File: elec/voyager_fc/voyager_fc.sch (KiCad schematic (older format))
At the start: 173 parts, among them J1 Raspberry Pi 5 Connector, J10 PWM Signal Rail 1, J11 BM03B-GHS-TBT_LF__SN__N_, J12 BM03B-GHS-TBT_LF__SN__N_, J13 BM03B-GHS-TBT_LF__SN__N_, J14 BM03B-GHS-TBT_LF__SN__N_, J15 Pi Power Connect, J16 AUX Power Connect, J17 BM04B-GHS-TBT_LF__SN__N_, J18 BM04B-GHS-TBT_LF__SN__N_, J19 BM04B-GHS-TBT_LF__SN__N_, J2 BM06B-GHS-TBT_LF__SN__N_, J20 BM04B-GHS-TBT_LF__SN__N_, J21 AUX Leak, J22 BM02B-GHS-TBT_LF__SN__N_, J23 BM02B-GHS-TBT_LF__SN__N_, J24 BM02B-GHS-TBT_LF__SN__N_, J3 BM06B-GHS-TBT_LF__SN__N_, J4 BM06B-GHS-TBT_LF__SN__N_, J5 PWM Power Rail 2, J6 PWM GND Rail 2, J7 PWM Signal Rail 2, J8 PWM Power Rail 1, J9 PWM GND Rail 1, Q1 BSS138, Q2 BSS138, Q3 MMBT3906, U1 BME680, U10 LTC4311CDC_TRMPBF, U11 AMS1117-3.3, U12 TCA9548APWR, U13 TXS0102YZP, U14 TXS0102YZP, U15 TXS0102YZP, U16 TXS0102YZP, U17 ICM-20948, U2 PCA9685PW, U3 PCA9685PW, U4 ADS1015IDGS, U5 TPS2121RUXR, U6 AMS1117-1.8, U7 LTC4311CDC_TRMPBF, U8 LTC4311CDC_TRMPBF, U9 LTC4311CDC_TRMPBF, X1 SG-8002CE

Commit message: Start schematic makeover with proper hierarchy
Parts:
- removed C1, C10, C11, C12, C13, C14, C15, C16, C17, C18, C19, C2, C20, C21, C25, C26, C27, C28, C30, C31, C32, C5, C8, C9: 10uF, Capacitor_SMD:C_0805_2012Metric, symbol Device:C_Small
- removed C22: 1nF, Capacitor_SMD:C_0603_1608Metric, symbol Device:C_Small
- removed C23, C29: 1uF, Capacitor_SMD:C_0603_1608Metric, symbol Device:C_Small
- removed C24, C33: 10uF, Capacitor_SMD:C_0603_1608Metric, symbol Device:C_Small
- removed C3, C6: 0.1uF, Capacitor_SMD:C_0603_1608Metric, symbol Device:C_Small
- removed C34, C35, C36, C37, C46, C47, C48, C49: 10uF, Capacitor_SMD:C_0504_1310Metric, symbol Device:C_Small
- removed C38, C39, C40, C41: 0.1uF, Capacitor_SMD:C_0504_1310Metric, symbol Device:C_Small
- removed C4, C7: 4700uF, Capacitor_THT:CP_Radial_D10.0mm_P5.00mm, symbol Device:C
- removed C54: 0.1uf, Capacitor_SMD:C_0603_1608Metric, symbol Device:C_Small
- removed D4: WHITE, LED_SMD:LED_0603_1608Metric, symbol Device:LED
- removed J10: PWM Signal Rail 1, Connector_PinHeader_2.54mm:PinHeader_1x16_P2.54mm_Vertical, symbol Connector_Generic:Conn_01x16
- removed J5: PWM Power Rail 2, Connector_PinHeader_2.54mm:PinHeader_1x16_P2.54mm_Vertical, symbol Connector_Generic:Conn_01x16
- removed J6: PWM GND Rail 2, Connector_PinHeader_2.54mm:PinHeader_1x16_P2.54mm_Vertical, symbol Connector_Generic:Conn_01x16
- removed J7: PWM Signal Rail 2, Connector_PinHeader_2.54mm:PinHeader_1x16_P2.54mm_Vertical, symbol Connector_Generic:Conn_01x16
- removed J8: PWM Power Rail 1, Connector_PinHeader_2.54mm:PinHeader_1x16_P2.54mm_Vertical, symbol Connector_Generic:Conn_01x16
- removed J9: PWM GND Rail 1, Connector_PinHeader_2.54mm:PinHeader_1x16_P2.54mm_Vertical, symbol Connector_Generic:Conn_01x16
- removed Q1, Q2: BSS138, Package_TO_SOT_SMD:SOT-23, symbol Transistor_FET:BSS138
- removed Q3: MMBT3906, Package_TO_SOT_SMD:SOT-23, symbol Transistor_BJT:MMBT3906
- removed R10, R11, R12, R13, R14, R15, R16, R17, R18, R19, R20, R23, R24, R25, R26, R27, R28, R29, R30, R31, R32, R33, R34, R35, R36, R37, R38, R5, R6, R7, R70, R8, R9: 220, Resistor_SMD:R_0603_1608Metric, symbol Device:R_Small
- removed R21: 200, Resistor_SMD:R_0603_1608Metric, symbol Device:R_Small
- removed R22, R4, R64, R65, R66, R67: 10k, Resistor_SMD:R_0603_1608Metric, symbol Device:R_Small
- removed R39: 19.6k, Resistor_SMD:R_0603_1608Metric, symbol Device:R_Small
- removed R40, R41, R42, R43, R46, R52, R53, R54, R55, R56, R57, R58, R59, R60, R61, R62, R63: 10k, Resistor_SMD:R_0402_1005Metric, symbol Device:R_Small
- removed R44: 4.99k, Resistor_SMD:R_0603_1608Metric, symbol Device:R_Small
- removed R45, R48: 1.15k, Resistor_SMD:R_0603_1608Metric, symbol Device:R_Small
- removed R47: 4.99K, Resistor_SMD:R_0603_1608Metric, symbol Device:R_Small
- removed R49: 4.32k, Resistor_SMD:R_0603_1608Metric, symbol Device:R_Small
- removed R50: 10.2k, Resistor_SMD:R_0603_1608Metric, symbol Device:R_Small
- removed R51: 36.5k, Resistor_SMD:R_0603_1608Metric, symbol Device:R_Small
- removed R68: 20K, Resistor_SMD:R_0603_1608Metric, symbol Device:R_Small
- removed R69: 1K, Resistor_SMD:R_0603_1608Metric, symbol Device:R_Small
- removed U1: BME680, Package_LGA:Bosch_LGA-8_3x3mm_P0.8mm_ClockwisePinNumbering, symbol Sensor:BME680
- removed U10, U7, U8, U9: LTC4311CDC_TRMPBF, DFN-6_DC, symbol LTC4311CDC_TRMPBF:LTC4311CDC_TRMPBF
- removed U11: AMS1117-3.3, Package_TO_SOT_SMD:SOT-223-3_TabPin2, symbol Regulator_Linear:AMS1117-3.3
- removed U12: TCA9548APWR, Package_SO:TSSOP-24_4.4x7.8mm_P0.65mm, symbol Interface_Expansion:TCA9548APWR
- removed U13, U14, U15, U16: TXS0102YZP, Package_BGA:Texas_DSBGA-8_0.9x1.9mm_Layout2x4_P0.5mm, symbol Logic_LevelTranslator:TXS0102YZP
- removed U17: ICM-20948, Sensor_Motion:InvenSense_QFN-24_3x3mm_P0.4mm, symbol Sensor_Motion:ICM-20948
- removed U2, U3: PCA9685PW, Package_SO:TSSOP-28_4.4x9.7mm_P0.65mm, symbol Driver_LED:PCA9685PW
- removed U4: ADS1015IDGS, Package_SO:TSSOP-10_3x3mm_P0.5mm, symbol Analog_ADC:ADS1015IDGS
- removed U5: TPS2121RUXR, IC_TPS2121RUXR, symbol TPS2121RUXR:TPS2121RUXR
- removed U6: AMS1117-1.8, Package_TO_SOT_SMD:SOT-223-3_TabPin2, symbol Regulator_Linear:AMS1117-1.8
- removed X1: SG-8002CE, Oscillator:Oscillator_SMD_SeikoEpson_SG8002CE-4Pin_3.2x2.5mm, symbol Oscillator:SG-8002CE
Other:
- moved on the sheet: C42, C43, C44, C45, C50, C51, C52, C53, J11, J12, J13, J14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

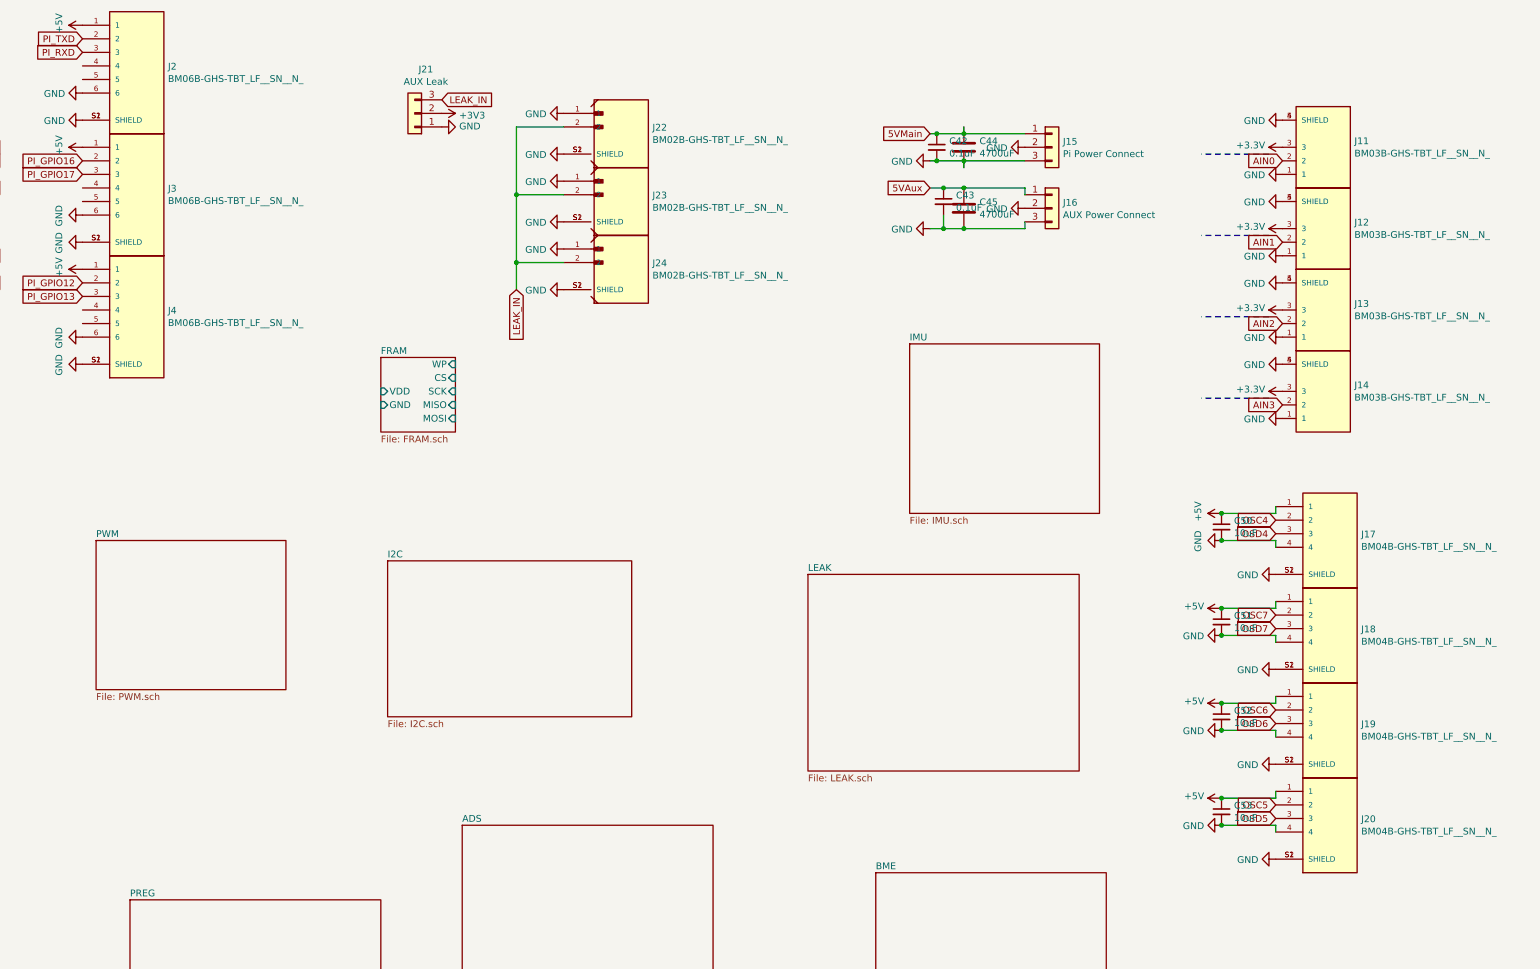
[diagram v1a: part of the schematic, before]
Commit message: Move connectors inside schematics
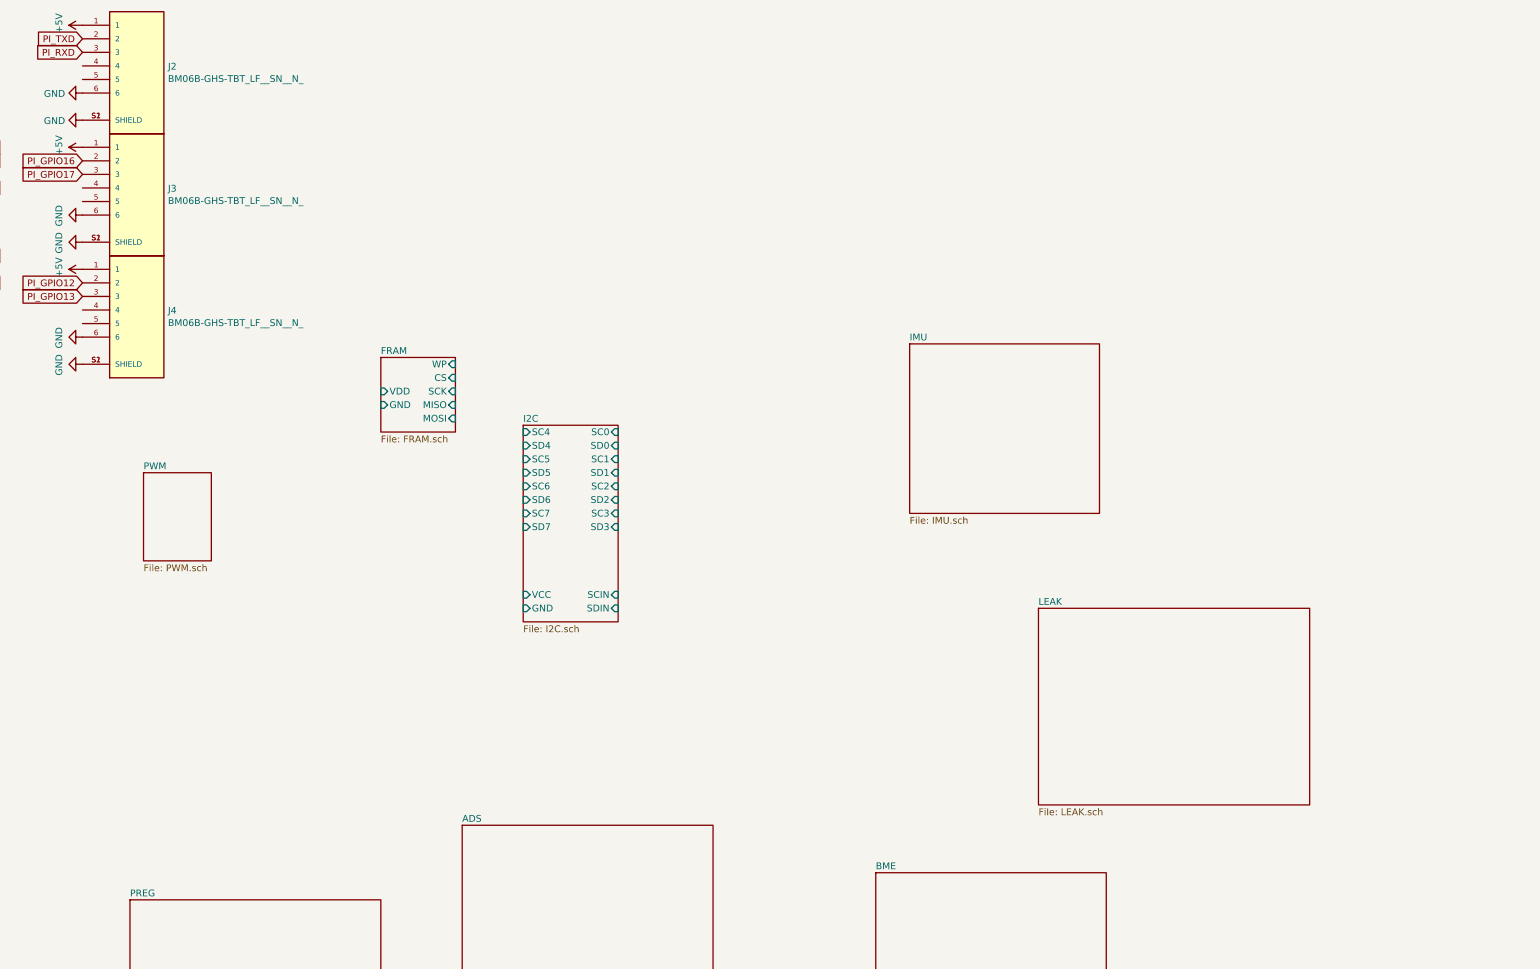
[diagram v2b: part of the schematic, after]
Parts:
- removed C42, C43: 0.1uF, Capacitor_SMD:C_0603_1608Metric, symbol Device:C_Small
- removed C44, C45: 4700uF, Capacitor_THT:CP_Radial_D10.0mm_P5.00mm, symbol Device:C
- removed C50, C51, C52, C53: 10uF, Capacitor_SMD:C_0504_1310Metric, symbol Device:C_Small
- removed J11, J12, J13, J14: BM03B-GHS-TBT_LF__SN__N_, CONN_BM03B-GHS-TBT_LF__SN__N_, symbol BM03B-GHS-TBT_LF__SN__N_:BM03B-GHS-TBT_LF__SN__N_
- removed J15: Pi Power Connect, Connector_PinHeader_2.54mm:PinHeader_1x03_P2.54mm_Vertical, symbol Connector_Generic:Conn_01x03
- removed J16: AUX Power Connect, Connector_PinHeader_2.54mm:PinHeader_1x03_P2.54mm_Vertical, symbol Connector_Generic:Conn_01x03
- removed J17, J18, J19, J20: BM04B-GHS-TBT_LF__SN__N_, JST_BM04B-GHS-TBT_LF__SN__N_, symbol BM04B-GHS-TBT_LF__SN__N_:BM04B-GHS-TBT_LF__SN__N_
- removed J21: AUX Leak, Connector_PinHeader_2.54mm:PinHeader_1x03_P2.54mm_Vertical, symbol Connector_Generic:Conn_01x03
- removed J22, J23, J24: BM02B-GHS-TBT_LF__SN__N_, JST_BM02B-GHS-TBT_LF__SN__N_, symbol BM02B-GHS-TBT_LF__SN__N_:BM02B-GHS-TBT_LF__SN__N_

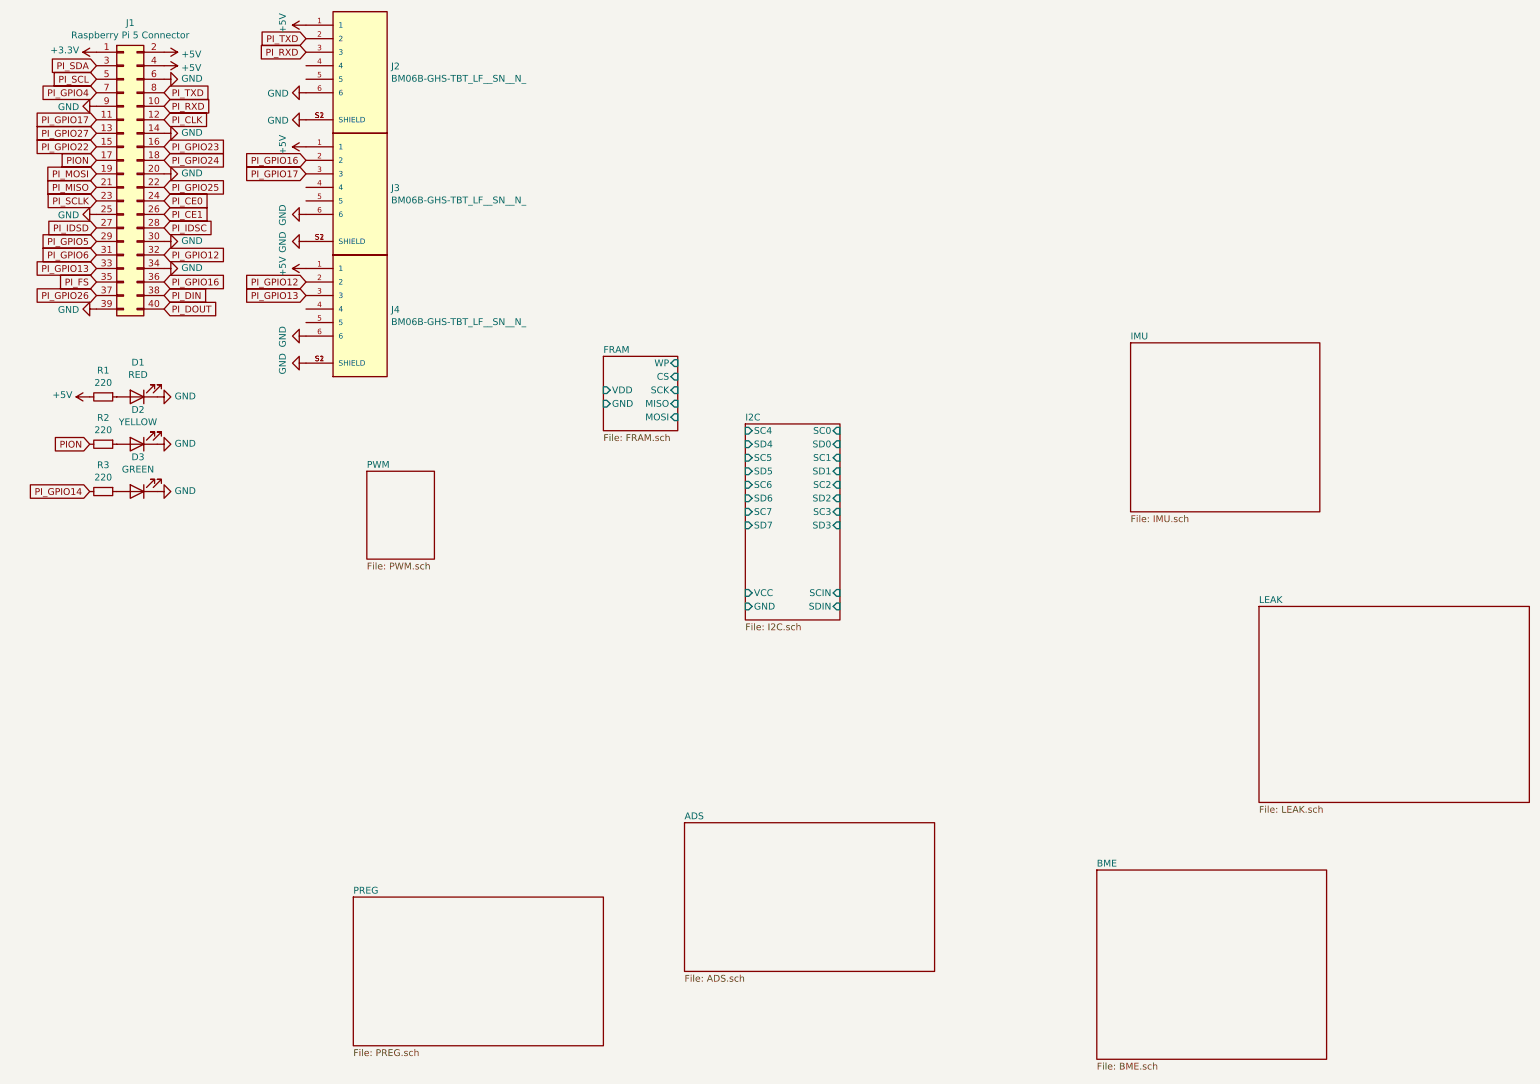
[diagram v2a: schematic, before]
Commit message: Place all components and start route
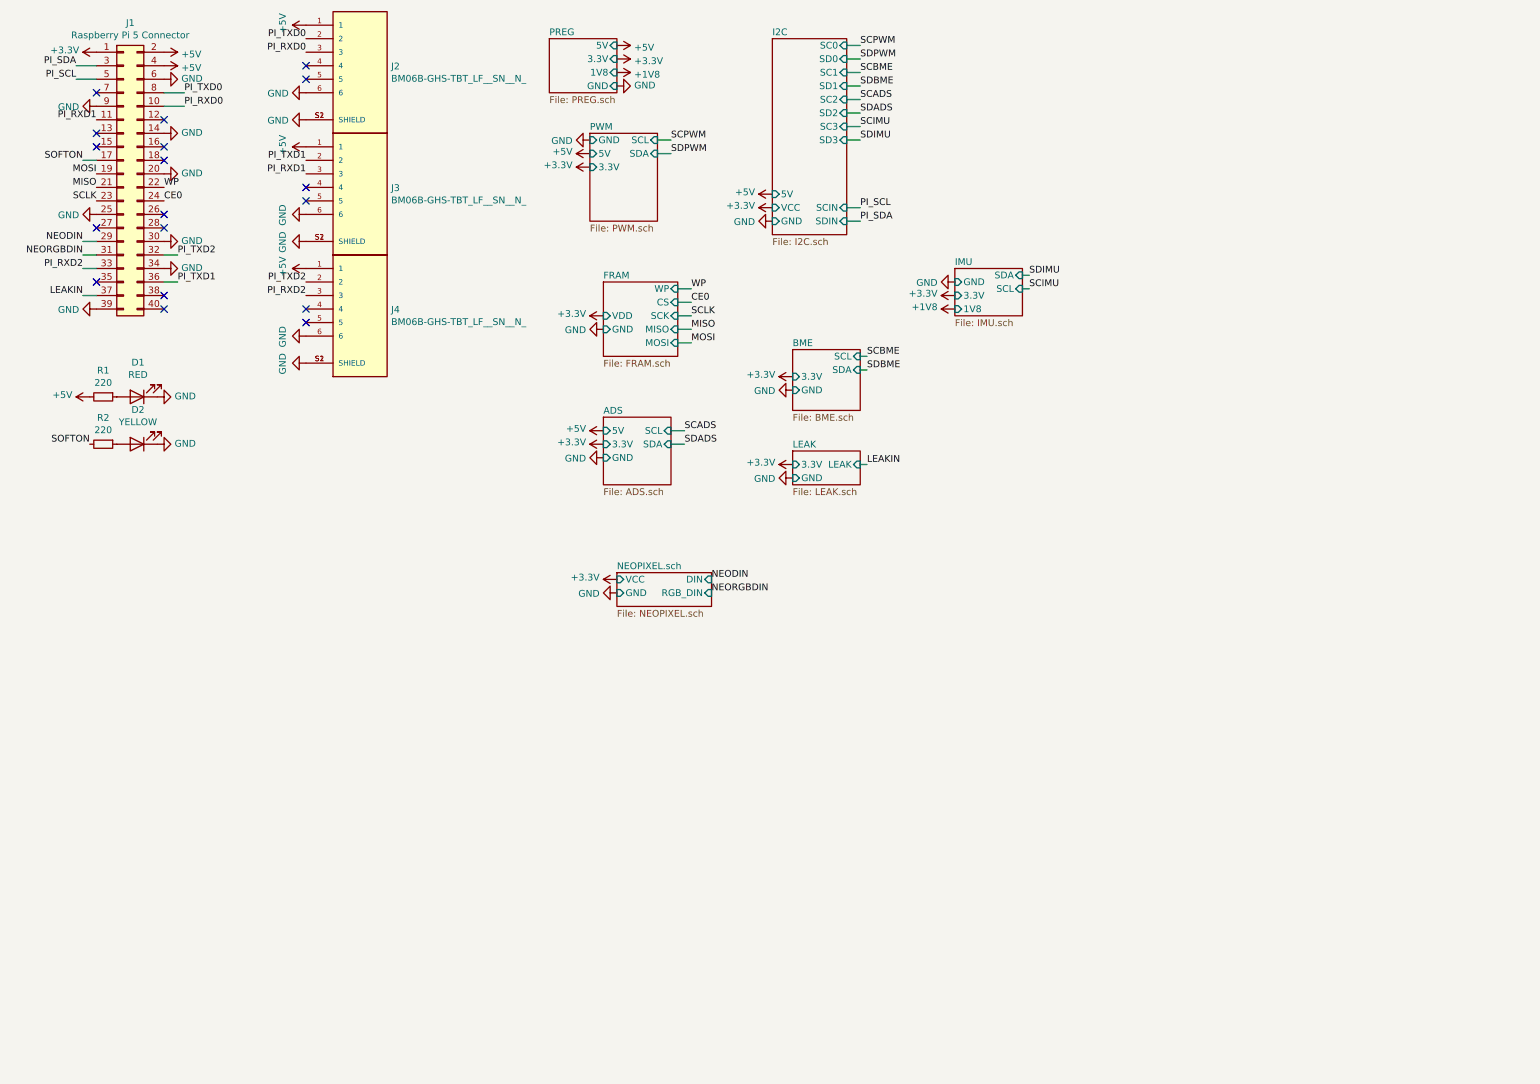
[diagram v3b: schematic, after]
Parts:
- removed D3: GREEN, LED_SMD:LED_0603_1608Metric, symbol Device:LED
- removed R3: 220, Resistor_SMD:R_0603_1608Metric, symbol Device:R_Small
- J2, J3, J4: footprint JST_BM06B-GHS-TBT_LF__SN__N_ -> BM06B-GHS-TBT_LF__SN__N_:JST_BM06B-GHS-TBT_LF__SN__N_
- R1, R2: footprint Resistor_SMD:R_0603_1608Metric -> Resistor_SMD:R_0402_1005Metric
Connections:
- net PION renamed SOFTON
- net PI_CE0 renamed CE0
- net PI_CE1: no longer names the net of J1.26 (Pin_26)
- net PI_CLK: no longer names the net of J1.12 (Pin_12)
- net PI_DIN: no longer names the net of J1.38 (Pin_38)
- net PI_DOUT: no longer names the net of J1.40 (Pin_40)
- net PI_FS: no longer names the net of J1.35 (Pin_35)
- net PI_GPIO12 renamed PI_TXD2
- net PI_GPIO13 renamed PI_RXD2
- net PI_GPIO16 renamed PI_TXD1
- net PI_GPIO17 renamed PI_RXD1
- net PI_GPIO22: no longer names the net of J1.15 (Pin_15)
- net PI_GPIO23: no longer names the net of J1.16 (Pin_16)
- net PI_GPIO24: no longer names the net of J1.18 (Pin_18)
- net PI_GPIO25 renamed WP
- net PI_GPIO26 renamed LEAKIN
- net PI_GPIO27: no longer names the net of J1.13 (Pin_13)
- net PI_GPIO4: no longer names the net of J1.7 (Pin_7)
- net PI_GPIO5 renamed NEODIN
- net PI_GPIO6 renamed NEORGBDIN
- net PI_IDSC: no longer names the net of J1.28 (Pin_28)
- net PI_IDSD: no longer names the net of J1.27 (Pin_27)
- net PI_MISO renamed MISO
- net PI_MOSI renamed MOSI
- net PI_RXD renamed PI_RXD0
- net PI_SCLK renamed SCLK
- net PI_TXD renamed PI_TXD0
- no-connect marks 0 -> 18
